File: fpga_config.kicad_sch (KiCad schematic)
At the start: 45 parts, among them CON1 SD_Card_DM3BT, J2 Connector_02x08, SW1 B3U-1000P, SW2 B3U-1000P, U40 W25Q128JV

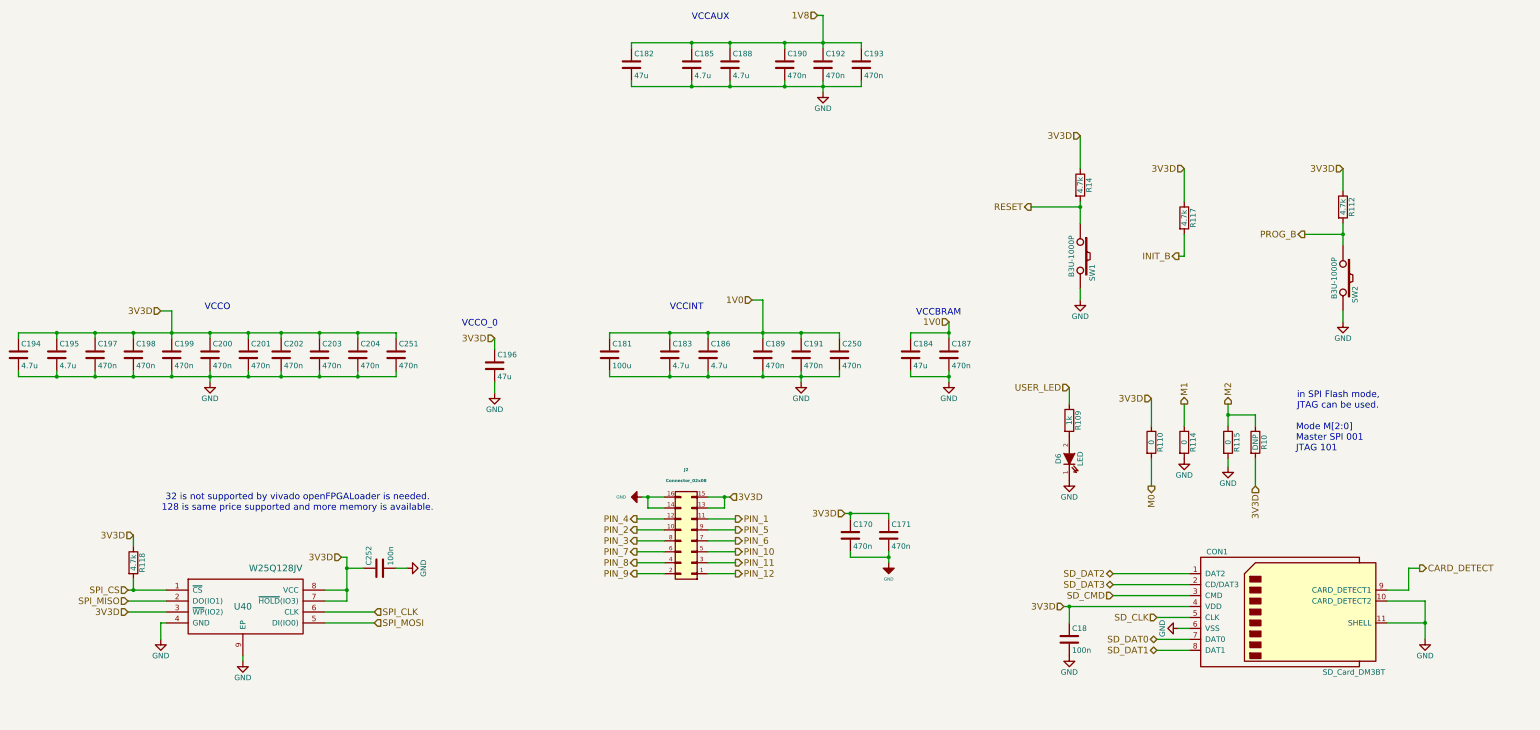
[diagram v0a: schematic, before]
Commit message: lt6232 is done with vias and copper pours are checked
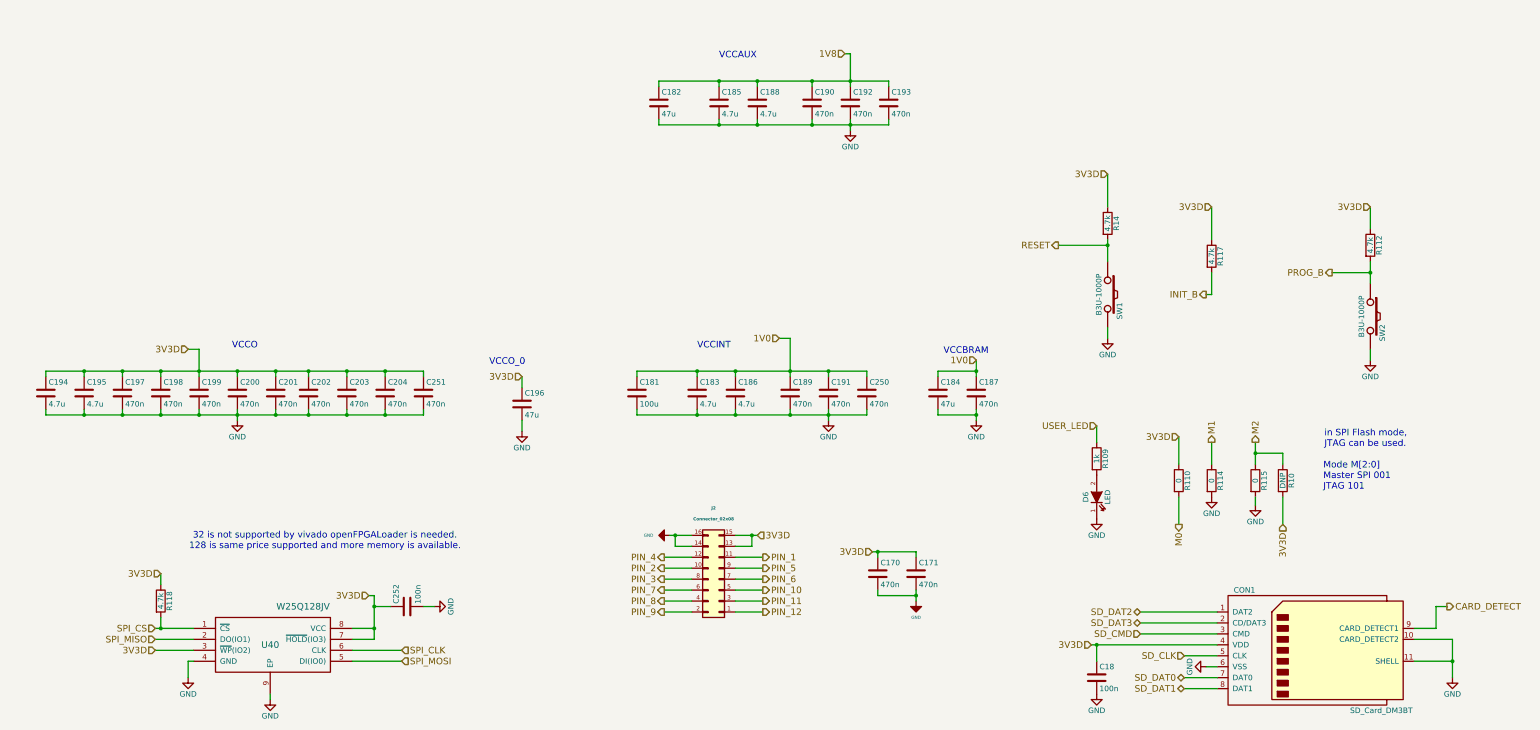
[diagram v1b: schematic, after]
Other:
- moved on the sheet: C170, C171, C18, C181, C182, C183, C184, C185, C186, C187, C188, C189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
